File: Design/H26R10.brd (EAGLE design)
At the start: 34.6 x 60 mm, 66 parts, among them P1 HEXABIT_17.32_X2_NO_P5_P10_P1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, U1 STM32F091RBT6STMICROELECTRONI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, U2 AD8275BRMZ, U3 ADR431ARMZ, U4 AD8295BCPZ-WP, U5 AD7687BRMZ, X1 XTALL_CSTCE8M00G52

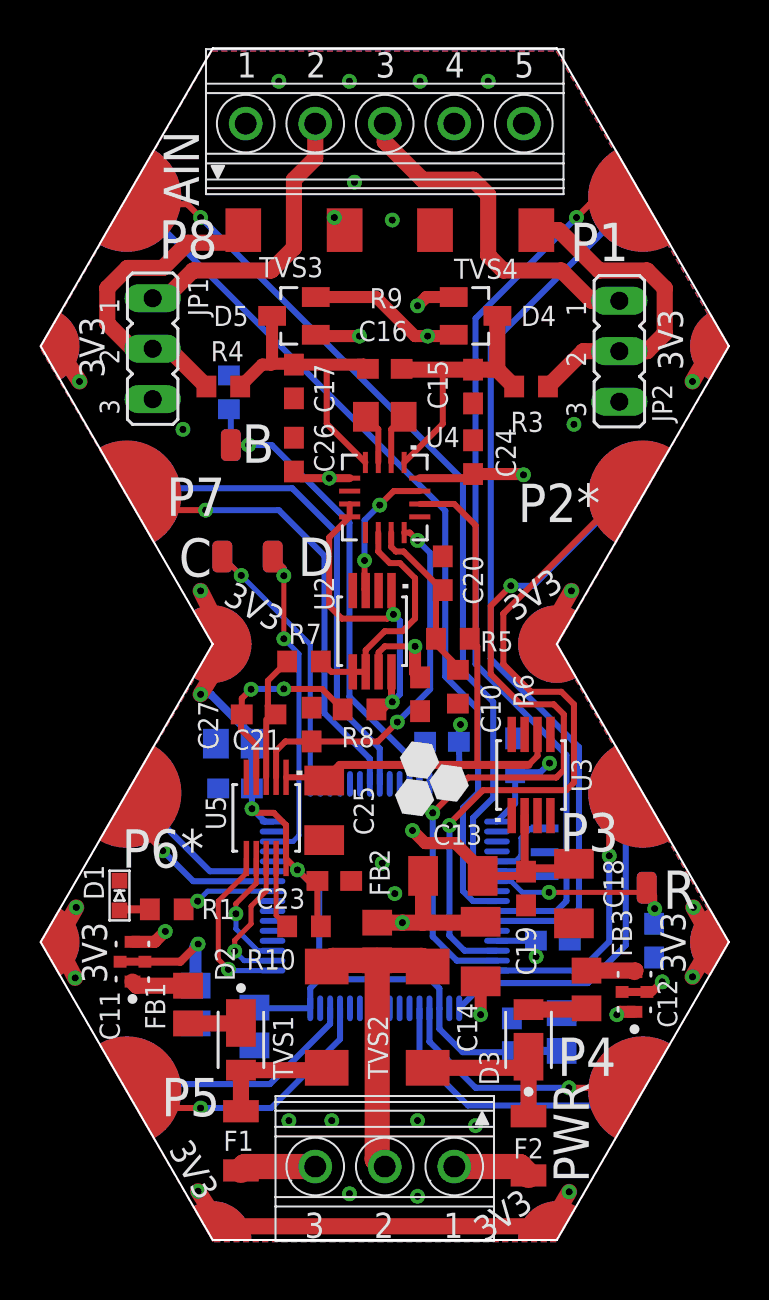
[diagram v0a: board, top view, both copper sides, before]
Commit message: Finished routing and silkscreen.. Reviewed ERC and DRC PCB is done
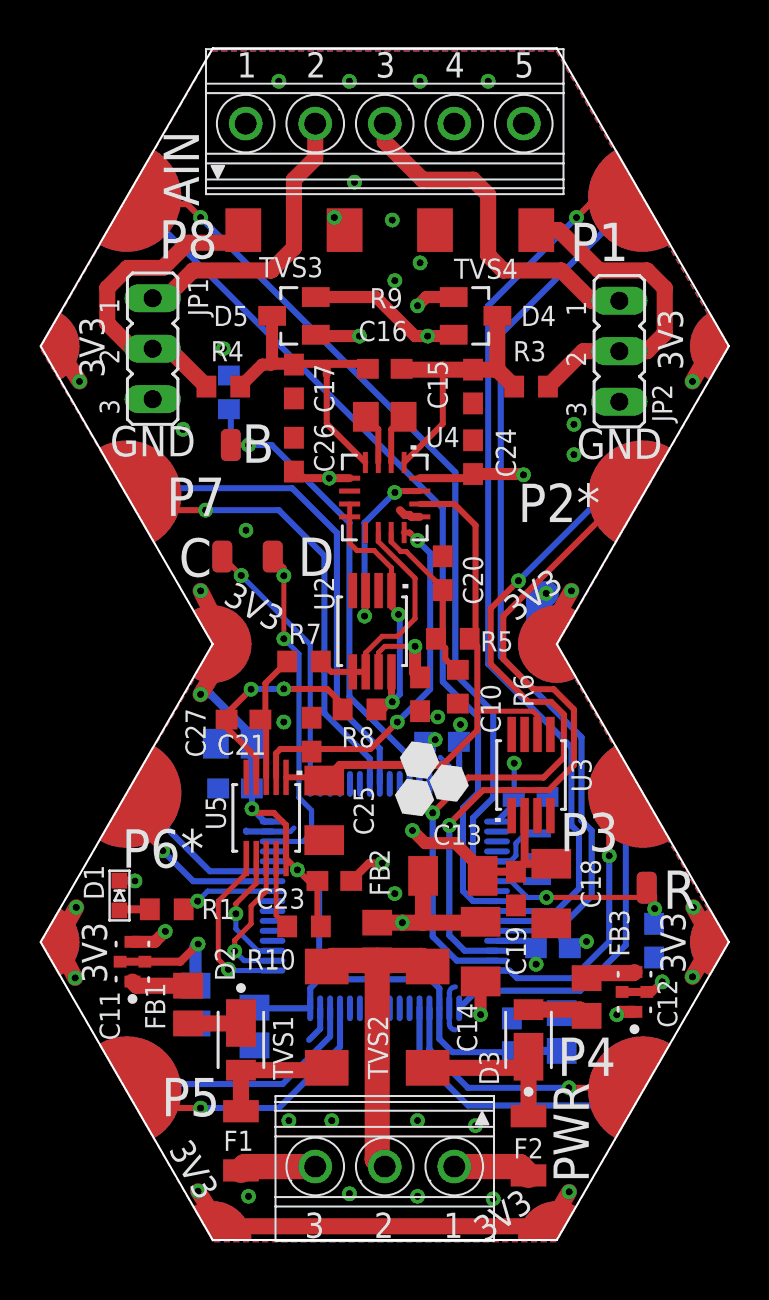
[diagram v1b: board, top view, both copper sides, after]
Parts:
- moved C9 2.24 mm to (30.3, 32.6), turned to 180 degrees
- moved C18 1.14 mm to (31.4, 27.7)
- moved C21 0.80 mm to (15.9, 36.4)
- moved C27 0.51 mm to (19.3, 35.7)
- moved C19 0.51 mm to (29.6, 27.9)
- moved X1 0.46 mm to (30.7, 29.5)
- moved C5 0.38 mm to (31.4, 24.9)
- moved FB3 0.38 mm to (33.1, 22.5)
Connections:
- net GND: now also U1.44, U1.45
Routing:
- net GND: track 0.00 -> 17.3 mm, vias 2 -> 13
- net AD8295_A1O: track 19.0 -> 15.6 mm
- net AD8295_OUT: track 6.96 -> 9.45 mm
- net +2.5V: track 30.1 -> 28.7 mm
- net AGND: track 41.3 -> 42.5 mm, vias 18 -> 20
- net +15V: track 90.1 -> 89.1 mm
- net VDD: track 192.2 -> 193.1 mm
- net UART4_TX: track 35.4 -> 34.5 mm
- net N$7: track 17.2 -> 18.1 mm
- net N$28: track 10.0 -> 10.8 mm
- net UART4_RX: track 37.7 -> 37.0 mm
- net B1: track 25.6 -> 24.9 mm
- net N$5: track 3.61 -> 2.97 mm
